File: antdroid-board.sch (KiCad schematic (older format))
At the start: 53 parts, among them P1 CONN_01X02, Q1 BSS138, Q2 BSS138, U1 LM2678T-5.0, U2 LM2678T-5.0, U3 LM2675M-5

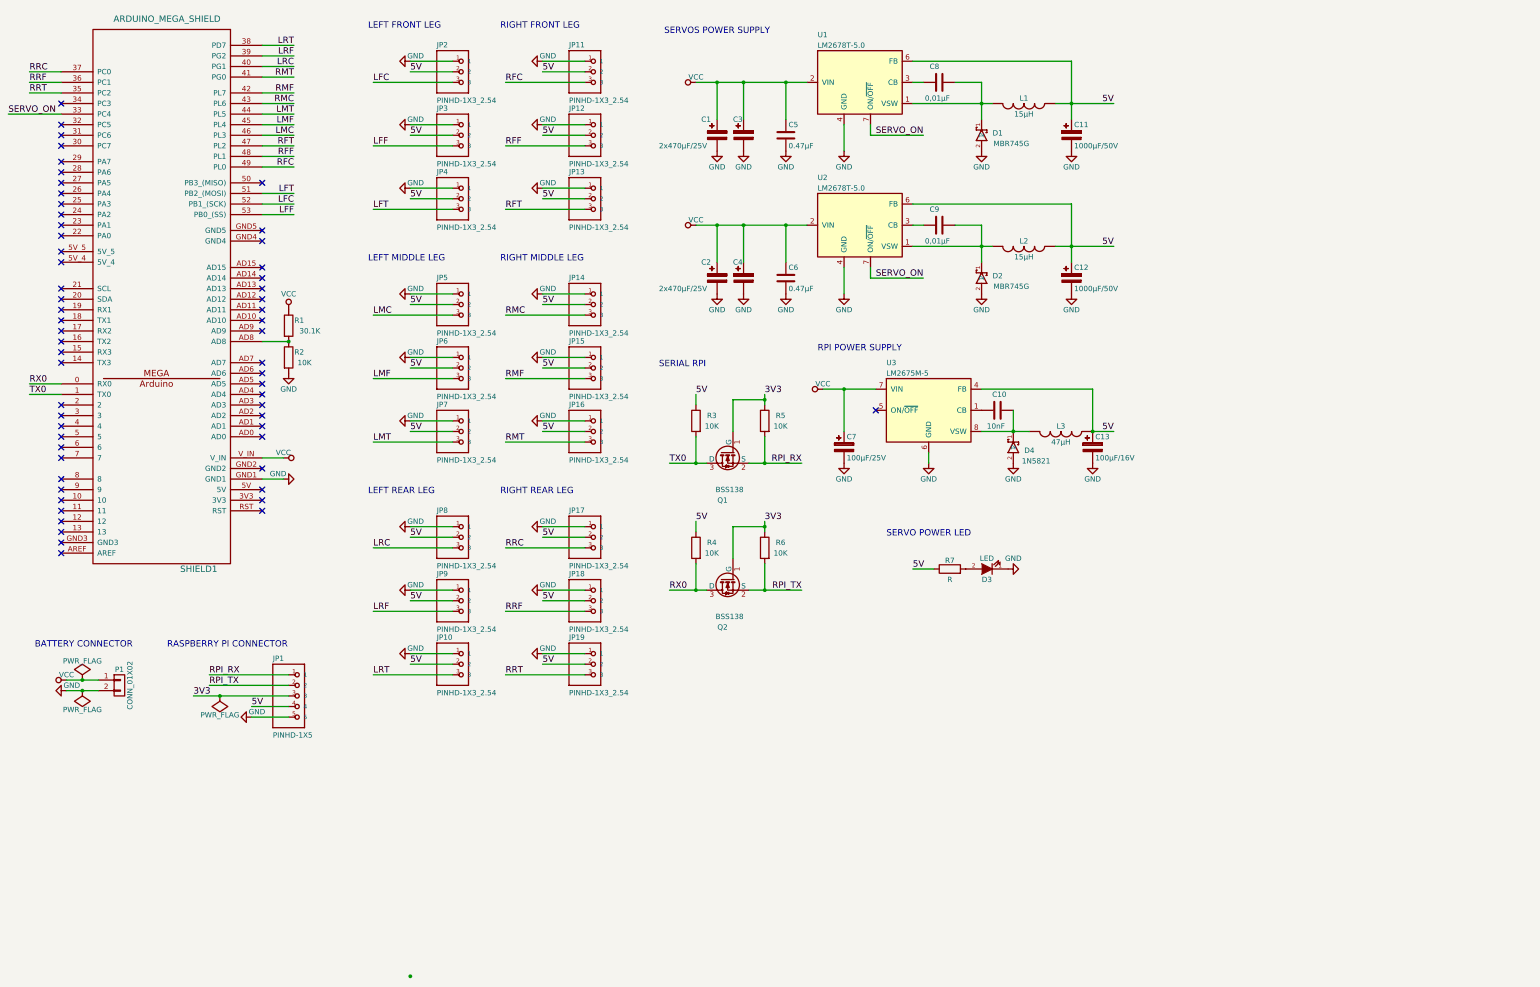
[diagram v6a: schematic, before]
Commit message: Finish footprint asign
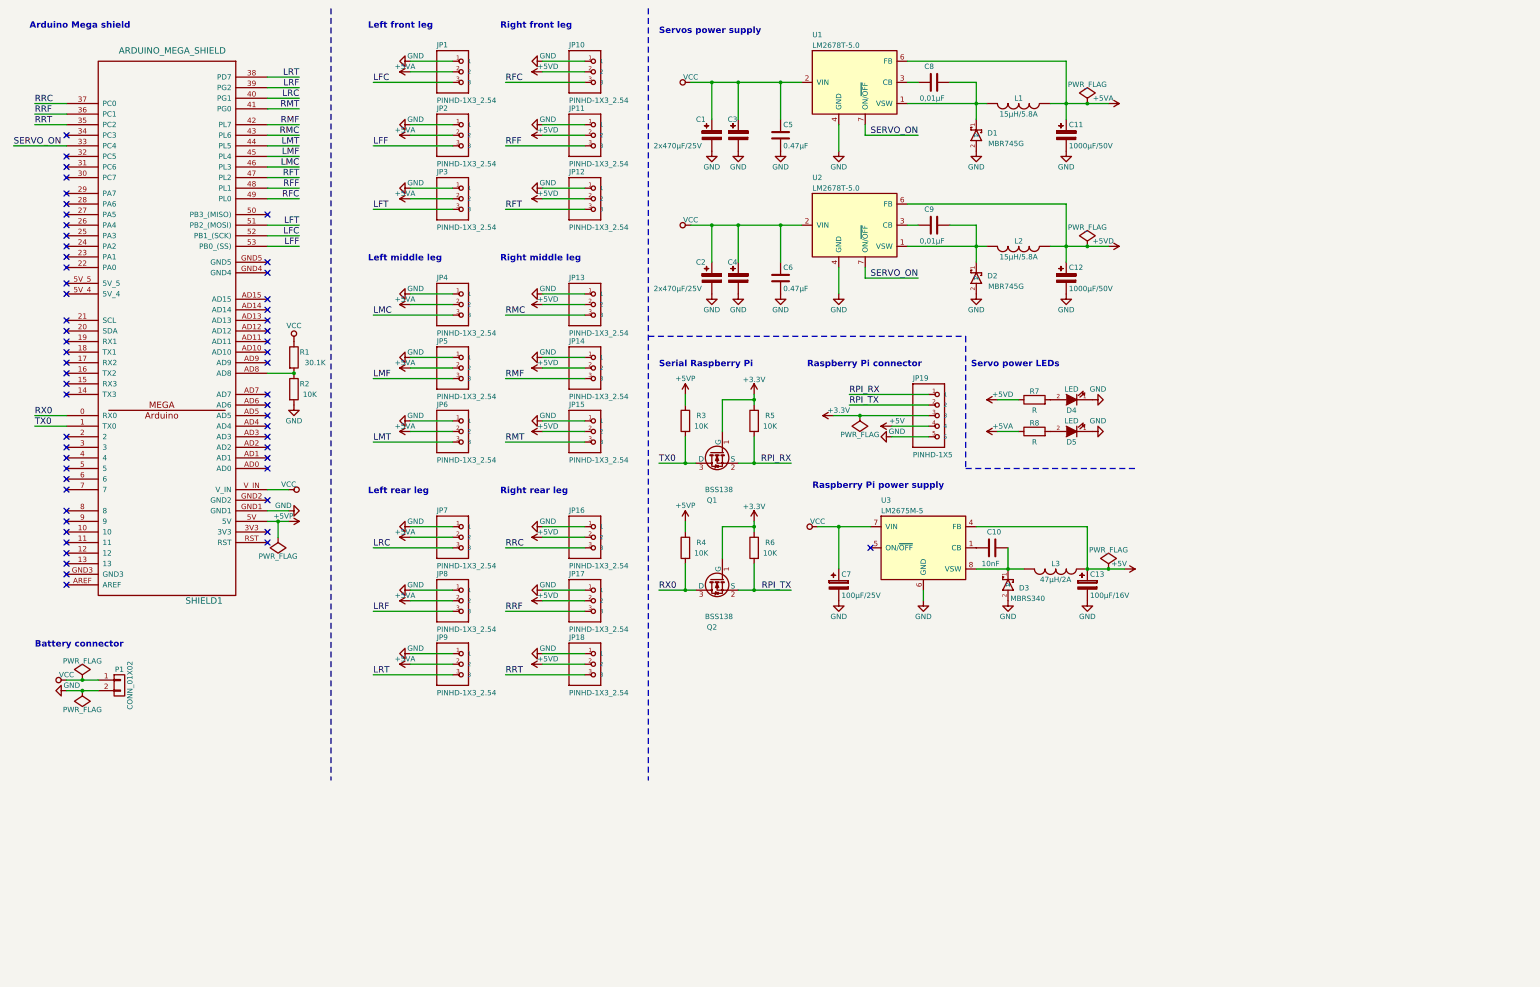
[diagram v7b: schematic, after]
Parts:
- added D5: LED, LEDs:LED-0603, symbol LED
- added R8: R, Resistors_SMD:R_0603_HandSoldering, symbol R
- C1, C2, C3, C4: footprint (none) -> Capacitors_ThroughHole:C_Radial_D10_L13_P5
- C10, C8, C9: footprint (none) -> Capacitors_SMD:C_0603_HandSoldering
- C11, C12: footprint (none) -> Capacitors_ThroughHole:C_Radial_D12.5_L25_P5
- C13: footprint (none) -> Capacitors_ThroughHole:C_Radial_D5_L11_P2
- C5, C6: footprint (none) -> Capacitors_ThroughHole:C_Disc_D6_P5
- C7: footprint (none) -> Capacitors_SMD:c_elec_6.3x7.7
- D1, D2: footprint DO-204AL -> Diodes_ThroughHole:Diode_TO-220_Vertical
- D3: renamed from D4; value 1N5821 -> MBRS340; footprint DO-204AL -> Diodes_SMD:Diode-DO-214AB_Handsoldering
- D4: renamed from D3; footprint (none) -> LEDs:LED-0603
- JP19: renamed from JP1; footprint pinhead-1X05 -> Pin_Headers:Pin_Header_Straight_1x05
- L1, L2: value 15µH -> 15µH/5.8A; footprint LCI-50 -> Inductors:SELF-WE-PD-XXL
- L3: value 47µH -> 47µH/2A; footprint (none) -> Inductors:SELF-WE-PD-XXL; Ref (none) -> CDRH124NP-470MC
- P1: footprint (none) -> Connect:AK300-2
- R1, R2, R3, R4, R5, R6, R7: footprint (none) -> Resistors_SMD:R_0603_HandSoldering
- renumbered JP2 to JP1, JP11 to JP10, JP12 to JP11, JP13 to JP12, JP14 to JP13, JP15 to JP14, JP16 to JP15, JP17 to JP16, JP18 to JP17, JP19 to JP18, JP3 to JP2, JP4 to JP3, JP5 to JP4, JP6 to JP5, JP7 to JP6, JP8 to JP7, JP9 to JP8, JP10 to JP9
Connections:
- net GND: now also D5.1 (K)
- net +5VP: now reaches SHIELD1.5V
- net +5VP: now also R3.1, R4.1
- net 3V3 renamed +3V3
- removed net 5V: C11.1, C12.1, C13.1, JP1.2, JP10.2, JP11.2, JP12.2, JP13.2, JP14.2, JP15.2, JP16.2, JP17.2, JP18.2, JP19.4, JP2.2, JP3.2, JP4.2, JP5.2, JP6.2, JP7.2, JP8.2, JP9.2, L1.1, L2.1, L3.1, R3.1, R4.1, R7.1, U1.6 (FB), U2.6 (FB), U3.4 (FB)
- new net: D5.2 (A), R8.2
- new net +5V: C13.1, JP19.4, L3.1, U3.4 (FB)
- new net +5VA: C11.1, JP1.2, JP2.2, JP3.2, JP4.2, JP5.2, JP6.2, JP7.2, JP8.2, JP9.2, L1.1, R8.1, U1.6 (FB)
- new net +5VD: C12.1, JP10.2, JP11.2, JP12.2, JP13.2, JP14.2, JP15.2, JP16.2, JP17.2, JP18.2, L2.1, R7.1, U2.6 (FB)
- no-connect marks 59 -> 58
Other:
- note added: "Arduino Mega shield"
- note added: "Battery connector"
- note added: "Left front leg"
- note added: "Left middle leg"
- note added: "Left rear leg"
- note added: "Raspberry Pi connector"
- note added: "Raspberry Pi power supply"
- note added: "Right front leg"
- note added: "Right middle leg"
- note added: "Right rear leg"
- note added: "Serial Raspberry Pi"
- note added: "Servo power LEDs"
- note added: "Servos power supply"
- note removed: "BATTERY CONNECTOR"
- note removed: "LEFT FRONT LEG"
- note removed: "LEFT MIDDLE LEG"
- note removed: "LEFT REAR LEG"
- note removed: "RASPBERRY PI CONNECTOR"
- note removed: "RIGHT FRONT LEG"
- note removed: "RIGHT MIDDLE LEG"
- note removed: "RIGHT REAR LEG"
- note removed: "RPI POWER SUPPLY"
- note removed: "SERIAL RPI"
- note removed: "SERVO POWER LED"
- note removed: "SERVOS POWER SUPPLY"
- moved on the sheet: C1, C10, C11, C12, C13, C2, C3, C4, C5, C6, C7, C8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

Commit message: Starting place components, some fingerprints fixed
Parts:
- U1, U2: footprint Power_Integrations:TO-220 -> Power_Integrations:TO-220-7C
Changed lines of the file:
@@
 LIBS:led_rgb
 LIBS:dc-dc
+LIBS:arduino_shieldsNCL
 LIBS:antdroid-board-cache
 EELAYER 25 0
@@
 F 0 "U1" H 8150 1650 50  0000 L CNN
 F 1 "LM2678T-5.0" H 8150 1550 50  0000 L CNN
-F 2 "Power_Integrations:TO-220" H 8850 850 50  0001 C CIN
-F 3 "" H 8550 1200 50  0000 C CNN
+F 2 "Power_Integrations:TO-220-7C" H 8850 850 50  0001 C CIN
+F 3 "www.ti.com/lit/ds/symlink/lm2678.pdf" H 8550 1200 50  0001 C CNN
 	1    8550 1200
 	1    0    0    -1
@@
 F 0 "U2" H 8150 3000 50  0000 L CNN
 F 1 "LM2678T-5.0" H 8150 2900 50  0000 L CNN
-F 2 "Power_Integrations:TO-220" H 8850 2200 50  0001 C CIN
-F 3 "" H 8550 2550 50  0000 C CNN
+F 2 "Power_Integrations:TO-220-7C" H 8850 2200 50  0001 C CIN
+F 3 "www.ti.com/lit/ds/symlink/lm2678.pdf" H 8550 2550 50  0001 C CNN
 	1    8550 2550
 	1    0    0    -1
@@
 Wire Wire Line
 	10000 5800 10000 5600
-Connection ~ 10000 5800
 Wire Wire Line
 	10750 5800 10750 5400
@@
 Text Notes 750  700  0    60   ~ 12
 Arduino Mega shield
+Connection ~ 10000 5800
 $EndSCHEMATC
